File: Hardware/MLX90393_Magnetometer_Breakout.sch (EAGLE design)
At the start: 16 parts, among them U1 MLX90393_MAGNETOMETER

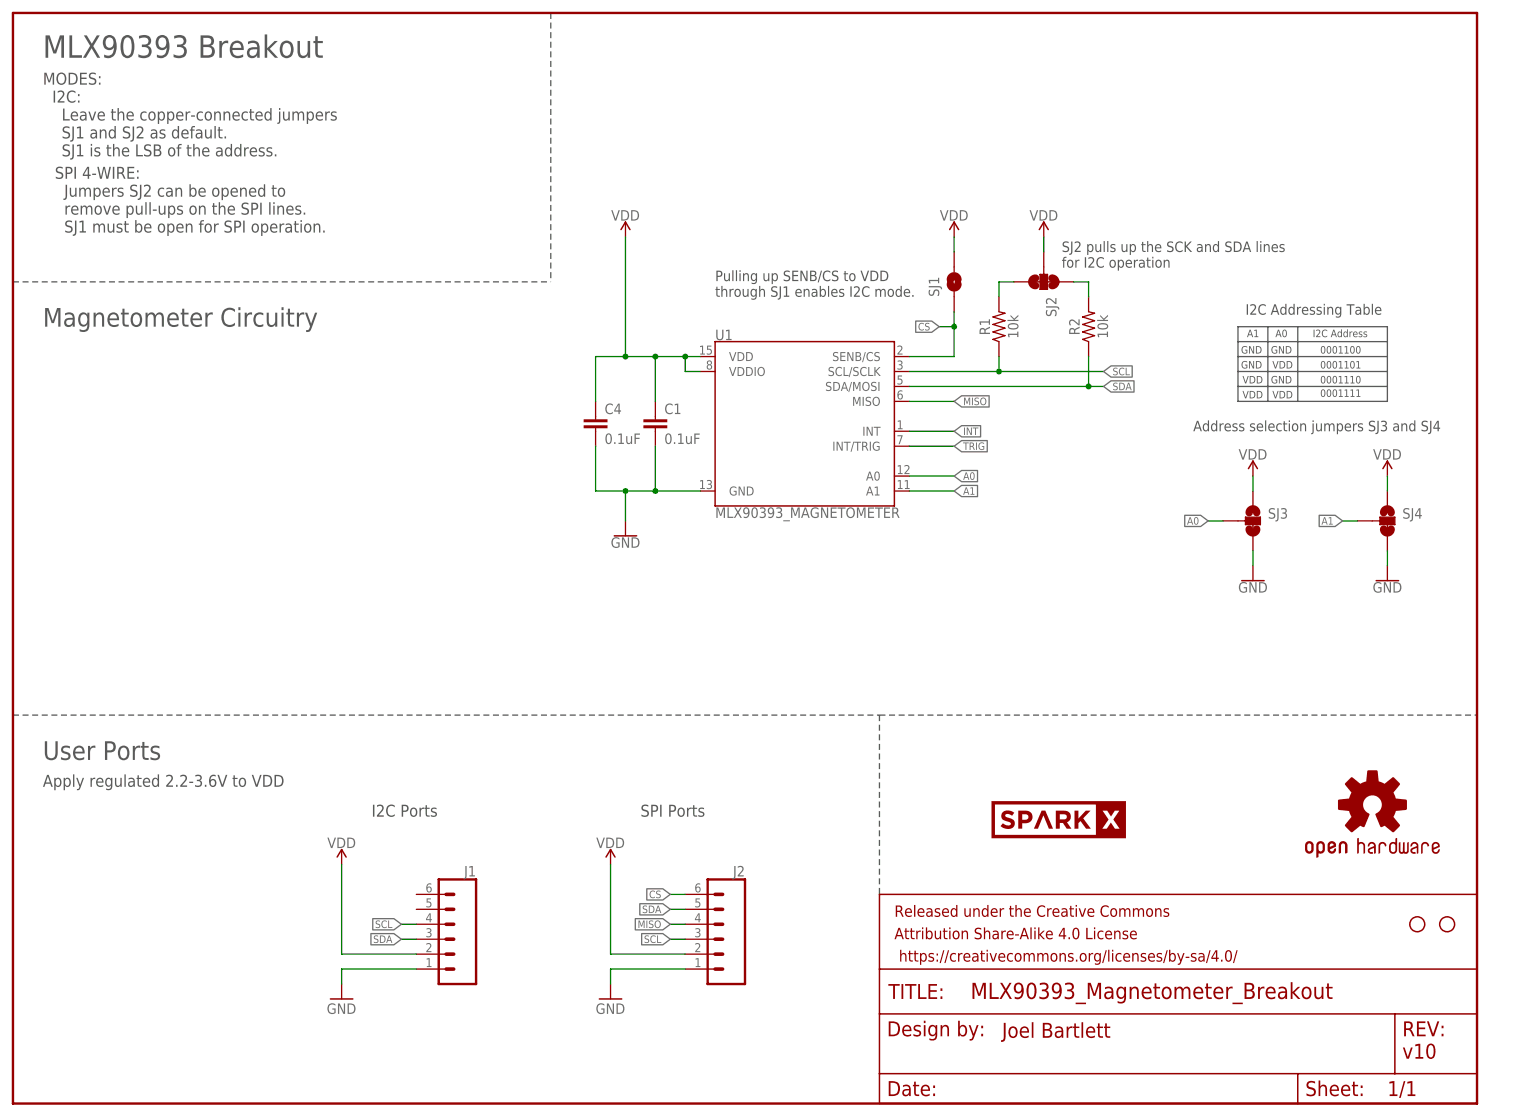
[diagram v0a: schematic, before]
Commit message: Production layout and panel for review
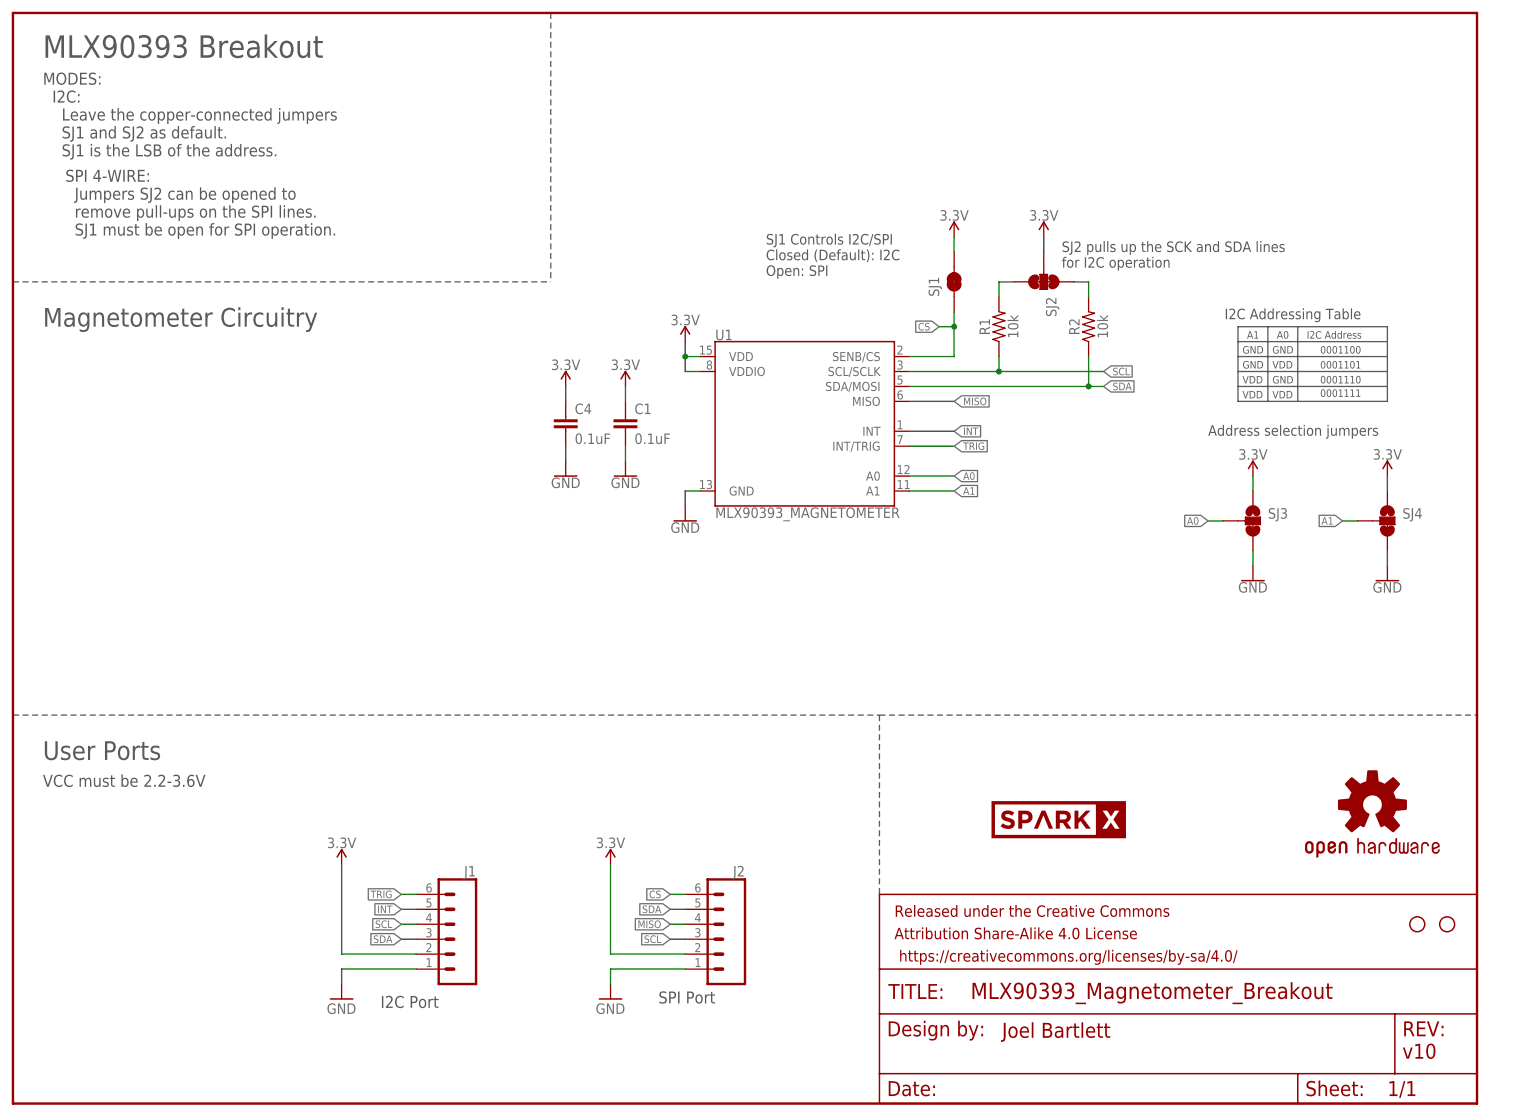
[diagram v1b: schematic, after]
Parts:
- SJ1: value SOLDERJUMPERTRACE -> JUMPER-SMT_2_NC_TRACE_SILK; device SparkFun:SOLDERJUMPERTRACE -> SparkFun-Jumpers:JUMPER-SMT_2_NC_TRACE_SILK
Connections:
- net VDD renamed 3.3V
- net INT: now also J1.5
- net TRIG: now also J1.6
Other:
- note added: "Address selection jumpers"
- note added: "I2C Port"
- note added: "SJ1 Controls I2C/SPI Closed (Default): I2C Open: SPI"
- note added: "SPI Port"
- note added: "VCC must be 2.2-3.6V"
- note removed: "Address selection jumpers SJ3 and SJ4"
- note removed: "Apply regulated 2.2-3.6V to VDD"
- note removed: "I2C Ports"
- note removed: "Pulling up SENB/CS to VDD through SJ1 enables I2C mode."
- note removed: "SPI Ports"
- moved on the sheet: C1, C4

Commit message: fixed silk and jumper
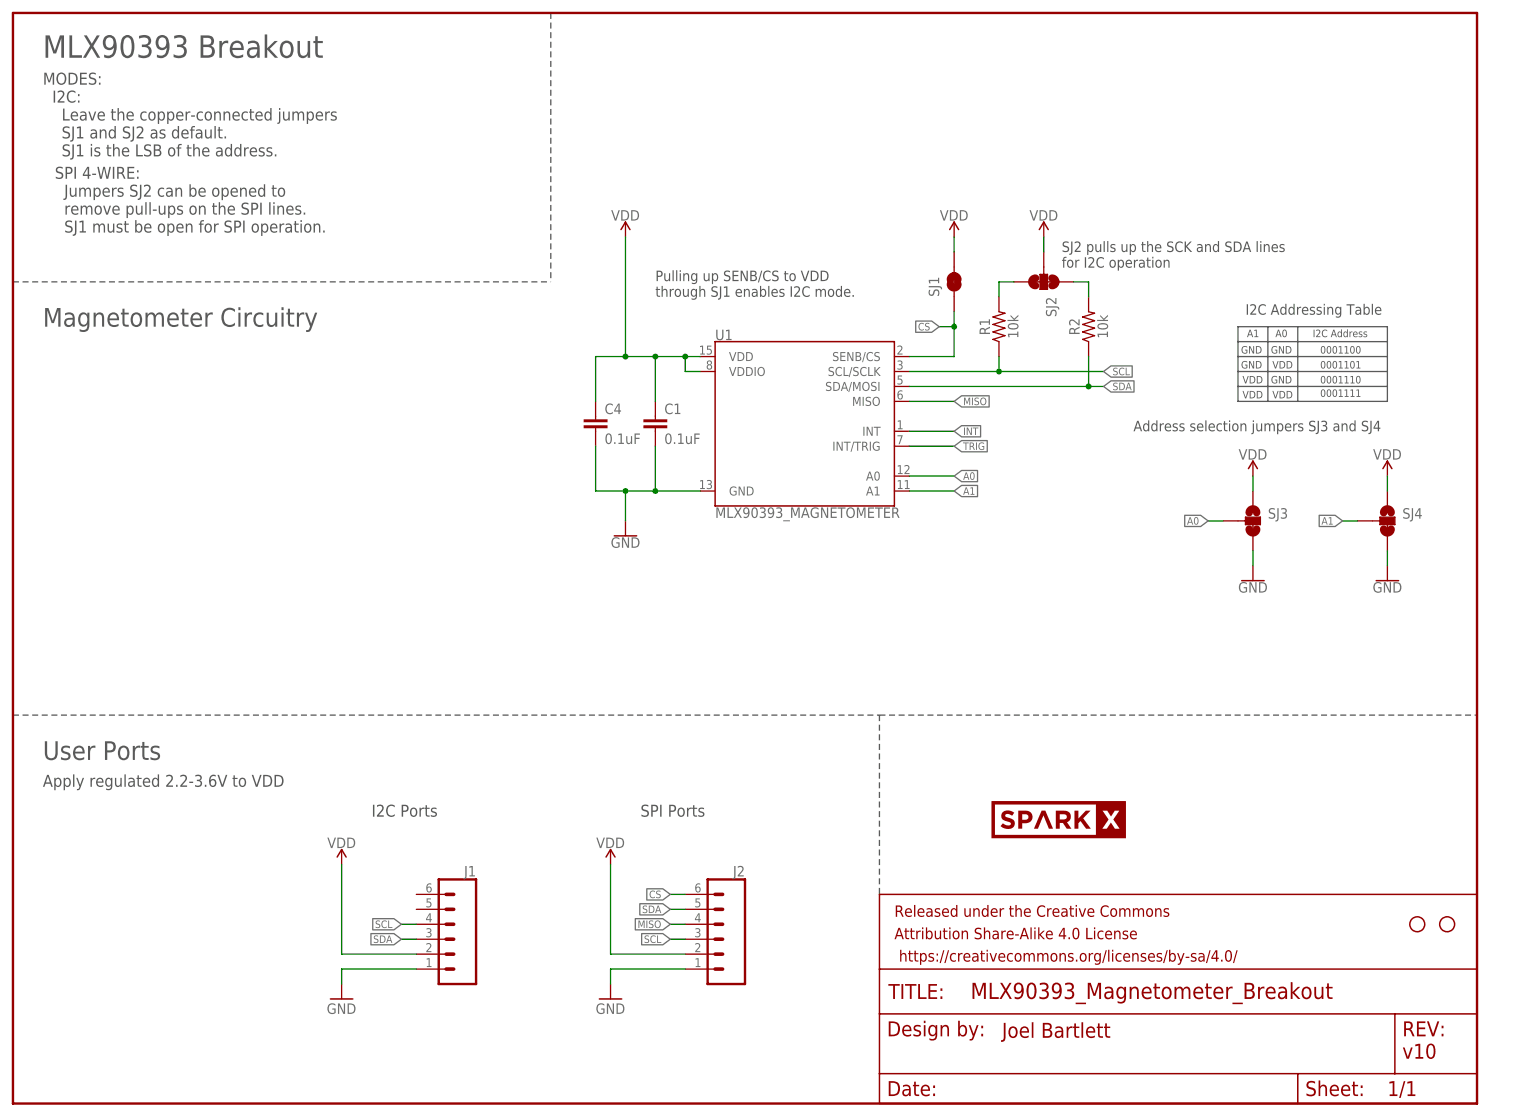
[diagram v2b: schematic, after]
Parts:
- removed U$1: OSHW-LOGOS, SparkFun:OSHW-LOGOS
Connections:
- net 3.3V renamed VDD
- net INT: no longer J1.5
- net TRIG: no longer J1.6
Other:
- note added: "Address selection jumpers SJ3 and SJ4"
- note added: "Apply regulated 2.2-3.6V to VDD"
- note added: "I2C Ports"
- note added: "Pulling up SENB/CS to VDD through SJ1 enables I2C mode."
- note added: "SPI Ports"
- note removed: "Address selection jumpers"
- note removed: "I2C Port"
- note removed: "SJ1 Controls I2C/SPI Closed (Default): I2C Open: SPI"
- note removed: "SPI Port"
- note removed: "VCC must be 2.2-3.6V"
- moved on the sheet: C1, C4
